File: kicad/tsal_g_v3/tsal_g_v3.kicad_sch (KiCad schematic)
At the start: 53 parts, among them J1 Conn_01x02_Pin, J2 Conn_01x02_Pin, J3 Conn_01x03, J4 Conn_01x06, Q1 2N7002, Q2 2N7002, Q3 MCT06P10-TP, U1 TL431LP, U2 LTV-817, U3 B1212, U4 BU4SU69G2, U5 BUS4S71G2, U6 BU4S81G2, U7 BU4S81G2, U8 BU4S01G2, U9 BU4S01G2

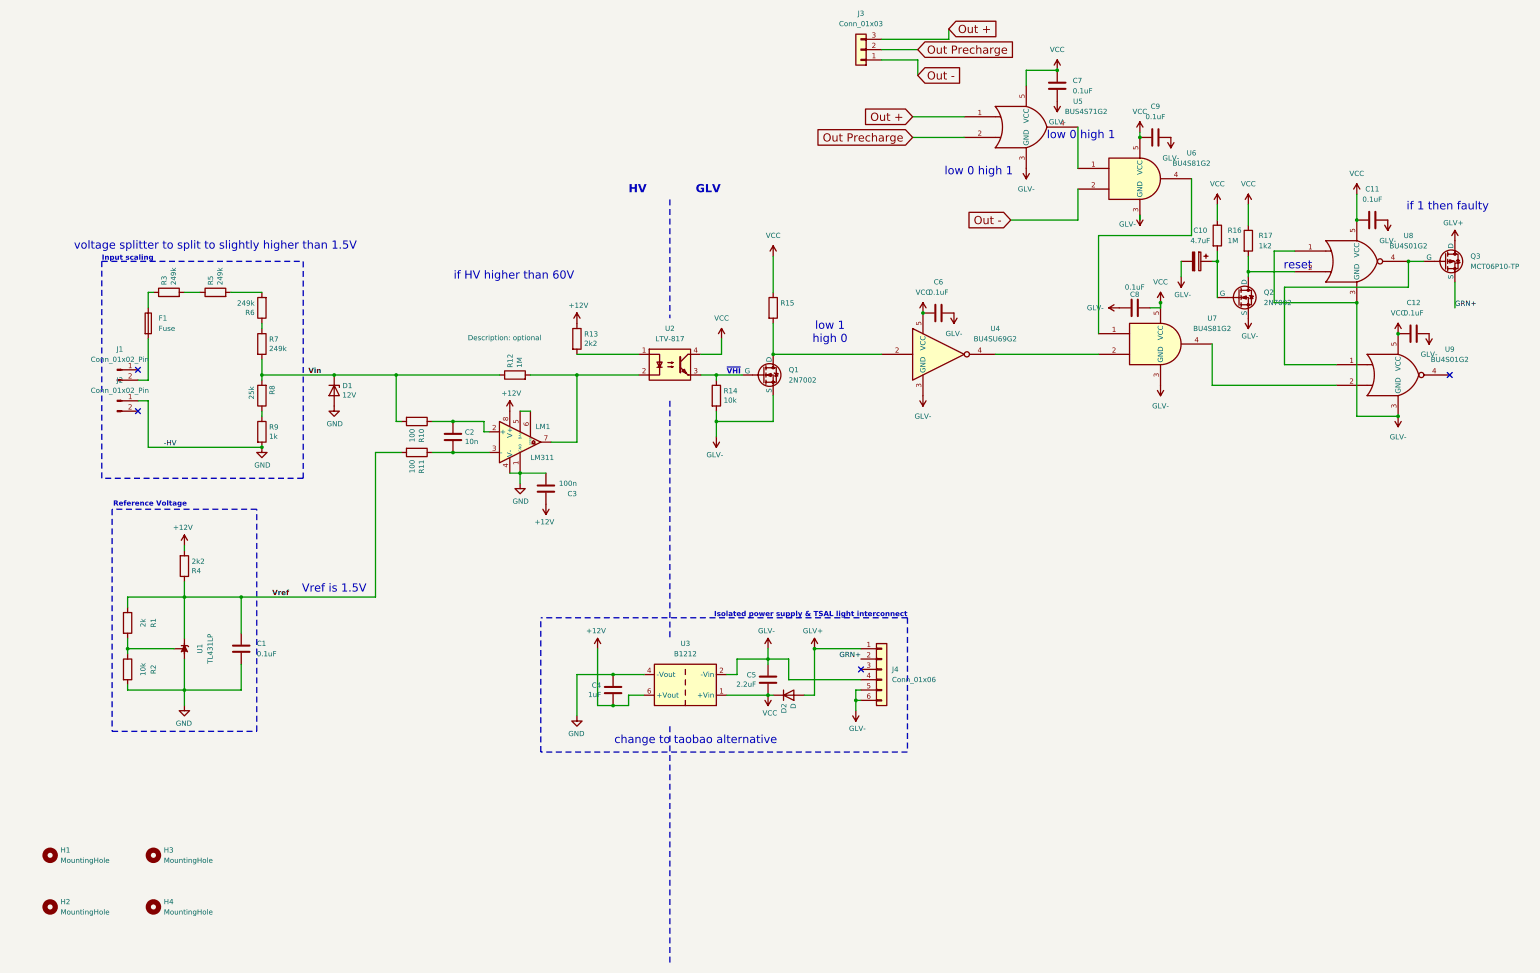
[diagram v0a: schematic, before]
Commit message: TSAL-G v3.0 New PCB design for TSAL-G, with changes for TLV431 for both TSAL-R and TSAL-G
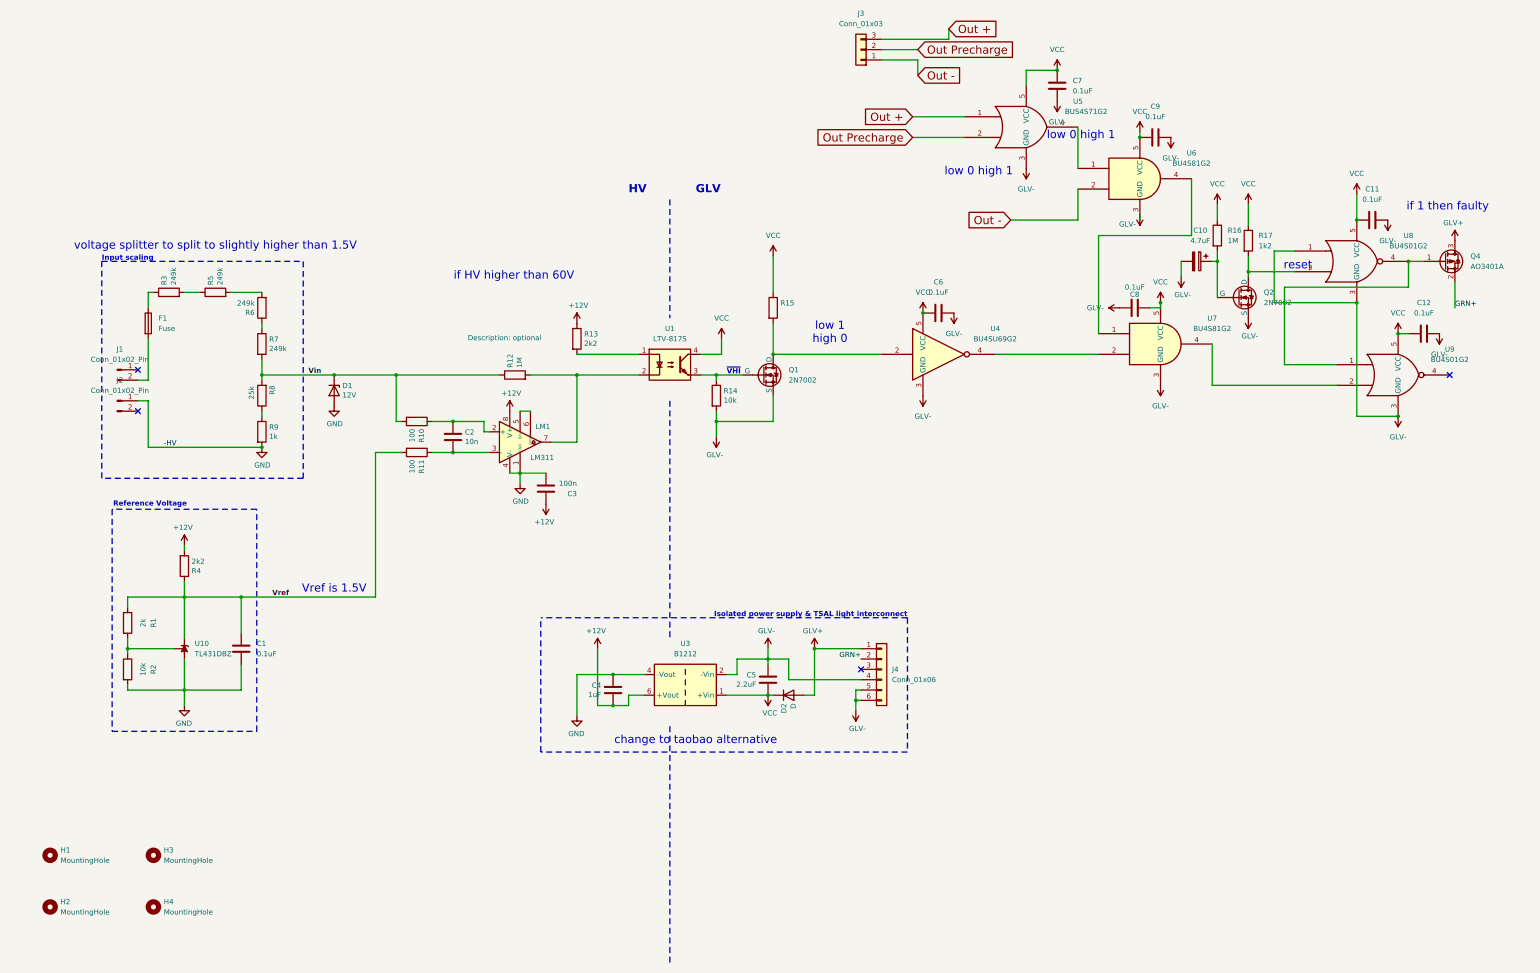
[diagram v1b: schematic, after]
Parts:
- removed Q3: MCT06P10-TP, Package_TO_SOT_SMD:SOT-223-3_TabPin2, symbol Simulation_SPICE:PMOS
- removed U1: TL431LP, Package_TO_SOT_THT:TO-92_Inline, symbol Reference_Voltage:TL431LP
- removed U2: LTV-817, Package_DIP:DIP-4_W7.62mm, symbol Isolator:LTV-817
- added Q4: AO3401A, Package_TO_SOT_SMD:SOT-23_Handsoldering, symbol Transistor_FET:AO3401A
- added U1: LTV-817S, Package_DIP:SMDIP-4_W9.53mm, symbol Isolator:LTV-817S
- added U10: TL431DBZ, Package_TO_SOT_SMD:SOT-23_Handsoldering, symbol Reference_Voltage:TL431DBZ
- C10: footprint Capacitor_SMD:C_1206_3216Metric_Pad1.33x1.80mm_HandSolder -> Capacitor_SMD:C_0805_2012Metric_Pad1.18x1.45mm_HandSolder
- F1: footprint Fuse:Fuse_1210_3225Metric -> Fuse:Fuse_0805_2012Metric_Pad1.15x1.40mm_HandSolder
- R10, R11, R12, R13, R14, R15, R16, R3, R4, R5, R6, R7, R8, R9: footprint Resistor_SMD:R_1206_3216Metric_Pad1.30x1.75mm_HandSolder -> Resistor_SMD:R_0805_2012Metric_Pad1.20x1.40mm_HandSolder
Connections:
- net GLV+: now also Q4.3 (D)
- net GND: now also U10.3 (A)
- net GRN+: now also Q4.2 (S)
- net VCC: now also U1.4
- net Vref: now also U10.1 (K)
- net at R13.2: now also U1.1
- net at LM1.7, R12.2: now also U1.2
- net at Q1.2 (G), R14.1: now also U1.3
- net at R1.2, R2.1: now also U10.2 (REF)
- net at U8.4, U9.1: now also Q4.1 (G)
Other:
- moved on the sheet: C12
